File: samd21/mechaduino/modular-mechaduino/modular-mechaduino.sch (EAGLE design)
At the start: 29 parts, among them J3 CONN_04SCREW_TERM, J4 USB4105-GF-A, J5 CONN_2X4LOCK, U1 UC_ATSAMD21E18AFAB, U2 A4950, U3 A4950, U4 AS5047

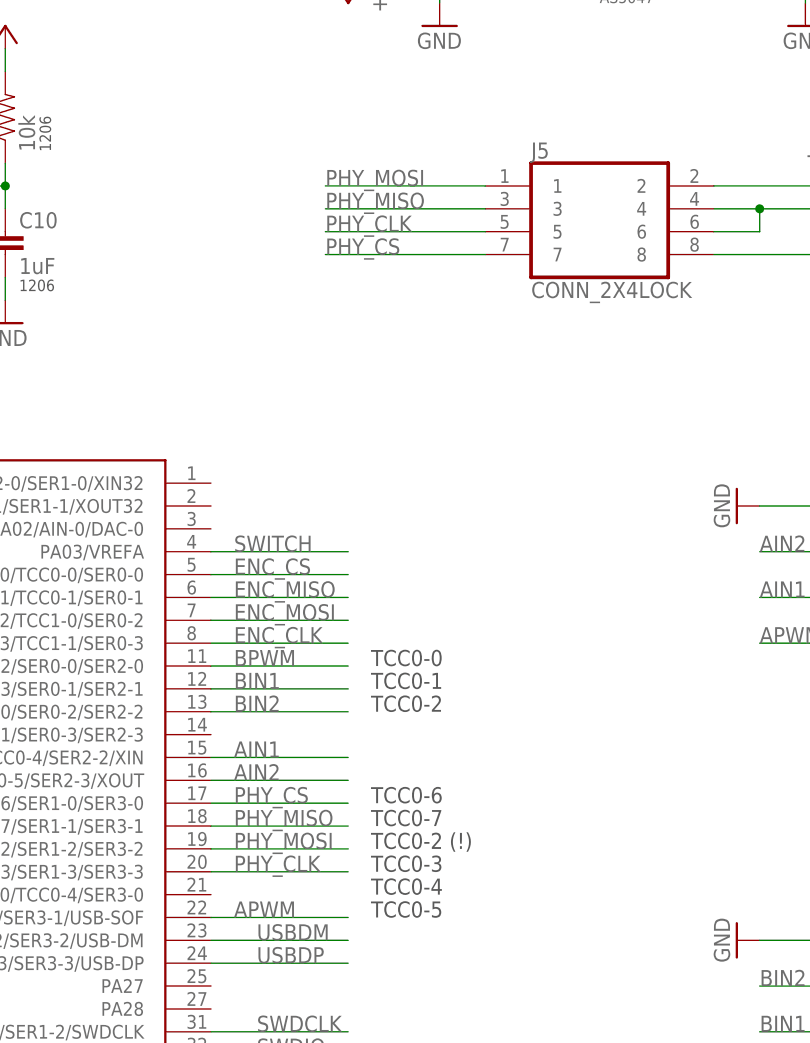
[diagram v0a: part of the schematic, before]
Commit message: pd hubs differentiated, rm mechaduino ref, add some bus backpacks
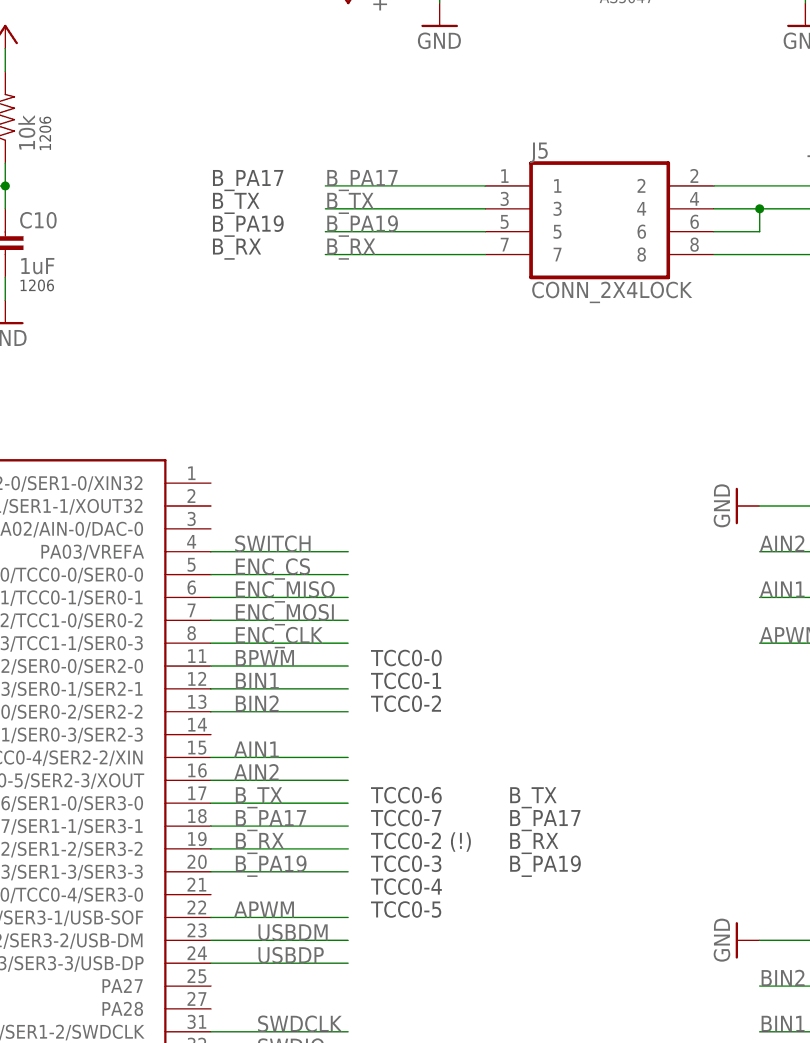
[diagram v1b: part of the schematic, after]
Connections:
- net PHY_CLK renamed B_PA19
- removed net PHY_CS: J5.7, U1.PA16/TCC2-0/TCC0-6/SER1-0/SER3-0
- removed net PHY_MISO: J5.3, U1.PA17/TCC2-1/TCC0-7/SER1-1/SER3-1
- removed net PHY_MOSI: J5.1, U1.PA18/TC3-0/TCC0-2/SER1-2/SER3-2
- new net B_PA17: J5.1, U1.PA17/TCC2-1/TCC0-7/SER1-1/SER3-1
- new net B_RX: J5.7, U1.PA18/TC3-0/TCC0-2/SER1-2/SER3-2
- new net B_TX: J5.3, U1.PA16/TCC2-0/TCC0-6/SER1-0/SER3-0
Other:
- note added: "B_PA17"
- note added: "B_PA19"
- note added: "B_RX"
- note added: "B_TX"
